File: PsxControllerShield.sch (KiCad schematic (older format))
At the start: 27 parts, among them J1 TO_PSX_PAD, J2 OSHW_LOGO, Q1 BSS138, Q2 BSS138, Q3 BSS138, Q4 BSS138, Q5 BSS138, U1 LM1117-3.3

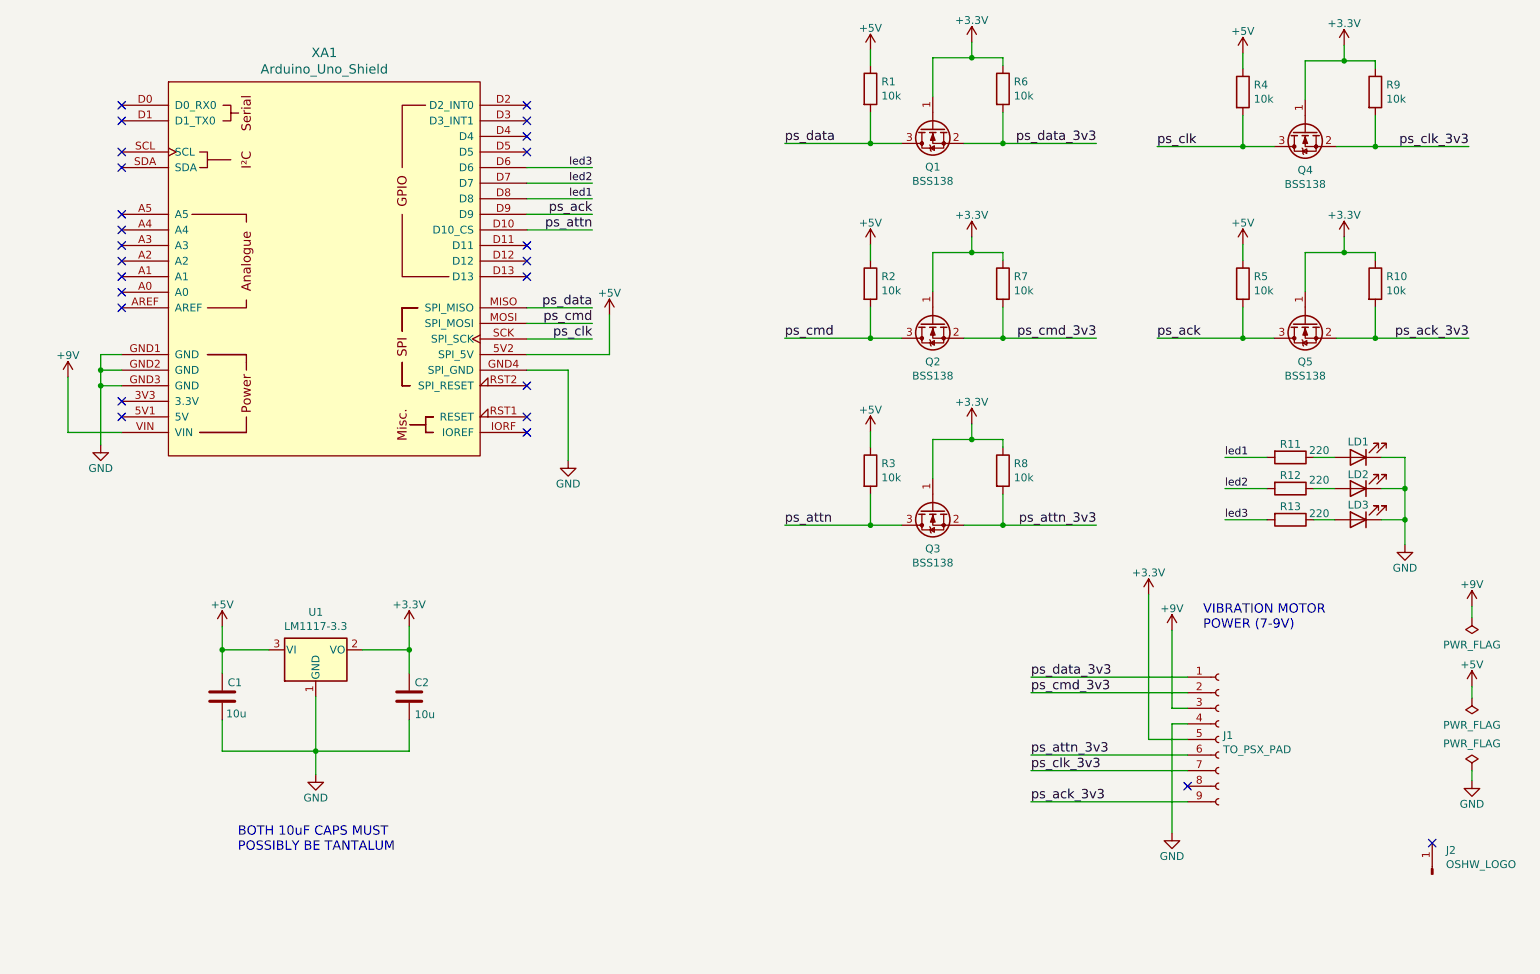
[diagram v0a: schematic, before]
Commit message: Ready for V2 (probably) Changes wrt V1: - Added 7.5V regulator for motors (I still think they're probably fine with 9V, but we want to be 100% rigorous with this board) - Move PSX connector towards board edge - Allow for actual tantalum caps - Reroute tracks - Switch all pullups to 1k, after measuring on a real PsOne
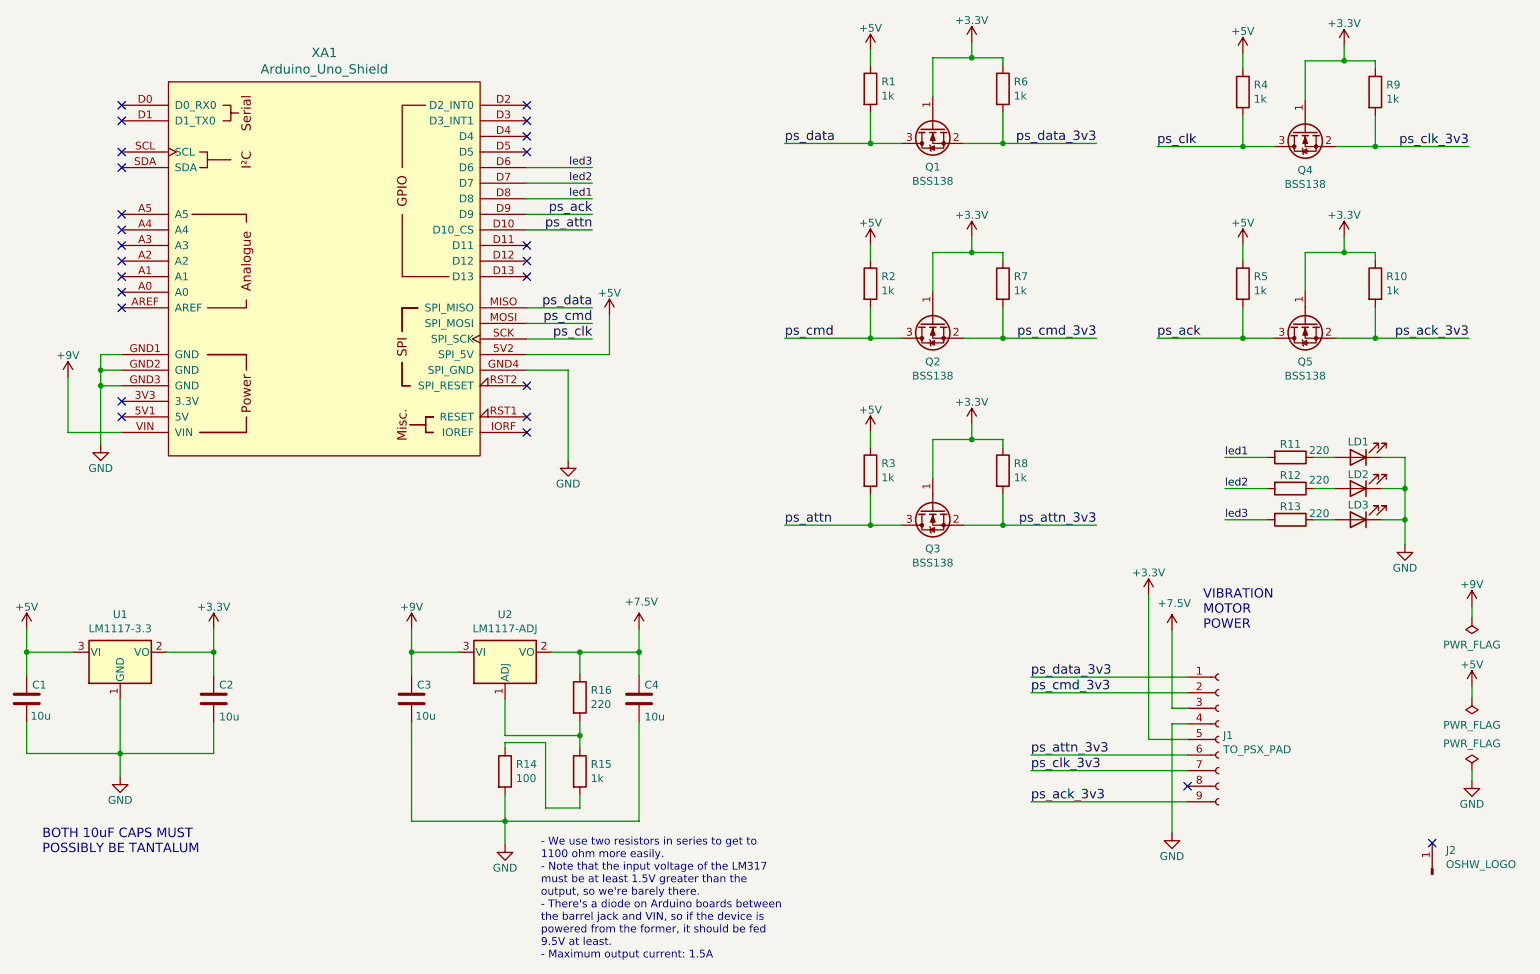
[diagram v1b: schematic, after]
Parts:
- added C3, C4: 10u, Capacitor_Tantalum_SMD:CP_EIA-3216-18_Kemet-A_Pad1.58x1.35mm_HandSolder, symbol Device:C
- added R14: 100, Resistor_SMD:R_0805_2012Metric_Pad1.20x1.40mm_HandSolder, symbol Device:R
- added R15: 1k, Resistor_SMD:R_0805_2012Metric_Pad1.20x1.40mm_HandSolder, symbol Device:R
- added R16: 220, Resistor_SMD:R_0805_2012Metric_Pad1.20x1.40mm_HandSolder, symbol Device:R
- added U2: LM1117-ADJ, Package_TO_SOT_SMD:SOT-223-3_TabPin2, symbol Regulator_Linear:LM1117-ADJ
- C1, C2: footprint Capacitor_SMD:C_1206_3216Metric_Pad1.42x1.75mm_HandSolder -> Capacitor_Tantalum_SMD:CP_EIA-3216-18_Kemet-A_Pad1.58x1.35mm_HandSolder
- J2: footprint Symbol:OSHW-Logo_7.5x8mm_Copper -> Symbol:OSHW-Logo_7.5x8mm_SilkScreen
- R1, R10, R2, R3, R4, R5, R6, R7, R8, R9: value 10k -> 1k; footprint Resistor_SMD:R_0805_2012Metric_Pad1.15x1.40mm_HandSolder -> Resistor_SMD:R_0805_2012Metric_Pad1.20x1.40mm_HandSolder
- R11, R12, R13: footprint Resistor_SMD:R_0805_2012Metric_Pad1.15x1.40mm_HandSolder -> Resistor_SMD:R_0805_2012Metric_Pad1.20x1.40mm_HandSolder
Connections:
- net +9V: now also C3.2, U2.3 (VI); no longer J1.3 (Pin_3)
- net GND: now also C3.1, C4.1, R14.2
- new net: R15.1, R16.2, U2.1 (ADJ)
- new net: R14.1, R15.2
- new net +7.5V: C4.2, J1.3 (Pin_3), R16.1, U2.2 (VO)
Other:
- note added: "- We use two resistors in series to get to\n1100 ohm more easily.\n- Note that the input voltage of the LM317\nmust be at least 1.5V greater than the\noutput, so we're barely there.\n- There's a diode on Arduino boards between\nthe barrel jack and VIN, so if the device is\npowered from the former, it should be fed\n9.5V at least.\n- Maximum output current: 1.5A"
- note added: "VIBRATION\nMOTOR\nPOWER"
- note removed: "VIBRATION MOTOR\nPOWER (7-9V)"
- moved on the sheet: C1, C2, U1

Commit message: Use larger footprint for tantalums
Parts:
- C1, C2, C3, C4: footprint Capacitor_Tantalum_SMD:CP_EIA-3216-18_Kemet-A_Pad1.58x1.35mm_HandSolder -> Capacitor_Tantalum_SMD:CP_EIA-3528-12_Kemet-T_Pad1.50x2.35mm_HandSolder
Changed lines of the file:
@@
 F 0 "C2" H 2680 5170 50  0000 R CNN
 F 1 "10u" H 2680 5375 50  0000 R CNN
-F 2 "Capacitor_Tantalum_SMD:CP_EIA-3216-18_Kemet-A_Pad1.58x1.35mm_HandSolder" H 2753 5110 50  0001 C CNN
+F 2 "Capacitor_Tantalum_SMD:CP_EIA-3528-12_Kemet-T_Pad1.50x2.35mm_HandSolder" H 2753 5110 50  0001 C CNN
 F 3 "~" H 2715 5260 50  0001 C CNN
 	1    2715 5260
@@
 F 0 "C1" H 1480 5170 50  0000 R CNN
 F 1 "10u" H 1490 5370 50  0000 R CNN
-F 2 "Capacitor_Tantalum_SMD:CP_EIA-3216-18_Kemet-A_Pad1.58x1.35mm_HandSolder" H 1553 5110 50  0001 C CNN
+F 2 "Capacitor_Tantalum_SMD:CP_EIA-3528-12_Kemet-T_Pad1.50x2.35mm_HandSolder" H 1553 5110 50  0001 C CNN
 F 3 "~" H 1515 5260 50  0001 C CNN
 	1    1515 5260
@@
 F 0 "C4" H 5410 5170 50  0000 R CNN
 F 1 "10u" H 5410 5375 50  0000 R CNN
-F 2 "Capacitor_Tantalum_SMD:CP_EIA-3216-18_Kemet-A_Pad1.58x1.35mm_HandSolder" H 5483 5110 50  0001 C CNN
+F 2 "Capacitor_Tantalum_SMD:CP_EIA-3528-12_Kemet-T_Pad1.50x2.35mm_HandSolder" H 5483 5110 50  0001 C CNN
 F 3 "~" H 5445 5260 50  0001 C CNN
 	1    5445 5260
@@
 F 0 "C3" H 3950 5170 50  0000 R CNN
 F 1 "10u" H 3960 5370 50  0000 R CNN
-F 2 "Capacitor_Tantalum_SMD:CP_EIA-3216-18_Kemet-A_Pad1.58x1.35mm_HandSolder" H 4023 5110 50  0001 C CNN
+F 2 "Capacitor_Tantalum_SMD:CP_EIA-3528-12_Kemet-T_Pad1.50x2.35mm_HandSolder" H 4023 5110 50  0001 C CNN
 F 3 "~" H 3985 5260 50  0001 C CNN
 	1    3985 5260

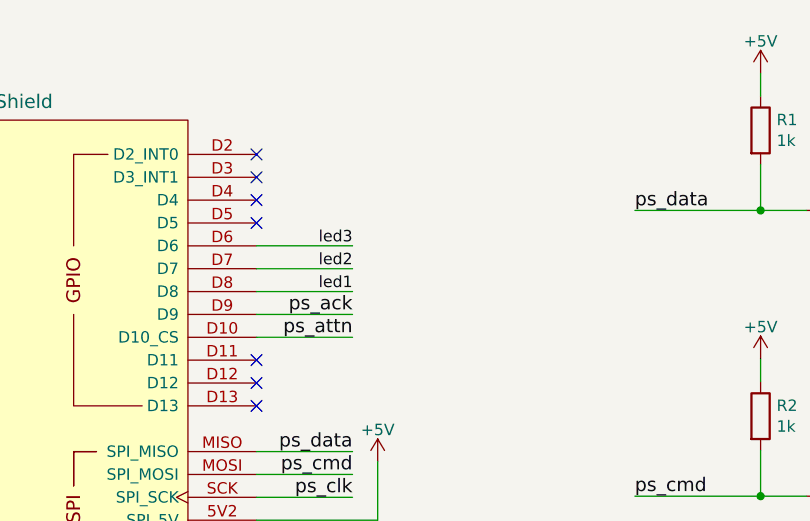
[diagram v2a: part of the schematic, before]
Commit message: Add ability to select ACK pin between 3 and 9
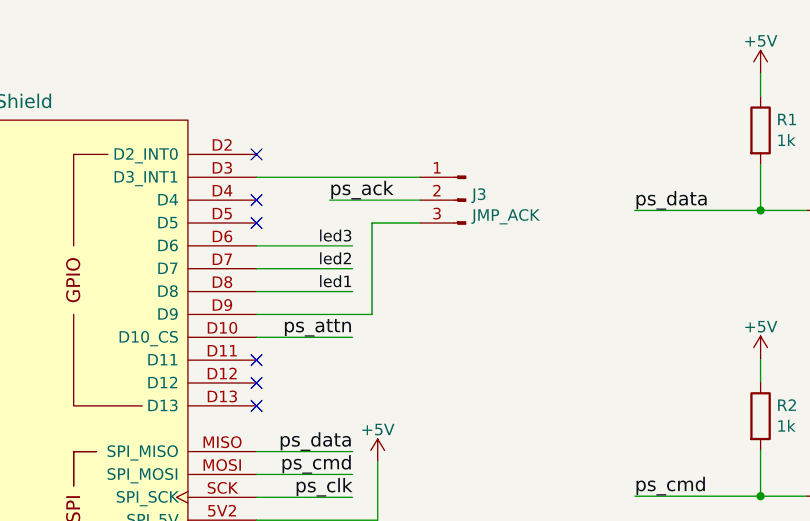
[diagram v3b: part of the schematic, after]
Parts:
- added J3: JMP_ACK, Connector_PinHeader_2.54mm:PinHeader_1x03_P2.54mm_Vertical, symbol Connector:Conn_01x03_Male
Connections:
- net ps_ack: now also J3.2 (Pin_2); no longer XA1.D9
- net at XA1.D3 (D3_INT1): now also J3.1 (Pin_1)
- new net: J3.3 (Pin_3), XA1.D9
- no-connect marks 25 -> 24
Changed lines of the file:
@@
 Sheet 1 1
 Title "PsxControllerShield"
-Date "2021-04-29"
+Date "2021-07-10"
 Rev "2"
 Comp "SukkoPera"
@@
 	5145 2950 4725 2950
 NoConn ~ 4725 1450
-NoConn ~ 4725 1550
 NoConn ~ 4725 1650
 NoConn ~ 4725 1750
@@
 Text Label 5145 2950 2    60   ~ 0
 ps_clk
-Wire Wire Line
-	5145 2150 4725 2150
-Text Label 5145 2150 2    60   ~ 0
+Text Label 5045 1650 0    60   ~ 0
 ps_ack
 Wire Wire Line
@@
 Text Notes 4815 6935 0    50   ~ 0
 - We use two resistors in series to get to\n1100 ohm more easily.\n- Note that the input voltage of the LM317\nmust be at least 1.5V greater than the\noutput, so we're barely there.\n- There's a diode on Arduino boards between\nthe barrel jack and VIN, so if the device is\npowered from the former, it should be fed\n9.5V at least.\n- Maximum output current: 1.5A
+Wire Wire Line
+	5440 1650 5045 1650
+Wire Wire Line
+	4725 1550 5440 1550
+Wire Wire Line
+	5230 2150 5230 1750
+Wire Wire Line
+	5230 1750 5440 1750
+Wire Wire Line
+	4725 2150 5230 2150
+$Comp
+L Connector:Conn_01x03_Male J3
+U 1 1 610B7C1A
+P 5640 1650
+F 0 "J3" H 5612 1674 50  0000 R CNN
+F 1 "JMP_ACK" H 5612 1583 50  0000 R CNN
+F 2 "Connector_PinHeader_2.54mm:PinHeader_1x03_P2.54mm_Vertical" H 5640 1650 50  0001 C CNN
+F 3 "~" H 5640 1650 50  0001 C CNN
+	1    5640 1650
+	-1   0    0    -1
+$EndComp
 $EndSCHEMATC
